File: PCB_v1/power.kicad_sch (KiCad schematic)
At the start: 23 parts, among them J2 S2B-PH-K-SLFSN, J3 Conn_01x05_Pin, J4 Conn_01x05_Pin, U1 BQ25185DLHR, U2 BQ27441-G1

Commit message: PCB changes before changing Seth's clock
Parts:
- U2: footprint Texas_S-PDSO-N12 -> Package_SON:Texas_S-PDSO-N12
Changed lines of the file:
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@@
 			)
 		)
-		(property "Description" "WSL0805R0100FEA1"
+		(property "Description" "Resistor"
 			(at 69.85 118.11 0)
 			(effects
@@
 			)
 		)
-		(property "Footprint" "Texas_S-PDSO-N12"
+		(property "Footprint" "Package_SON:Texas_S-PDSO-N12"
 			(at 101.6 129.54 0)
 			(effects

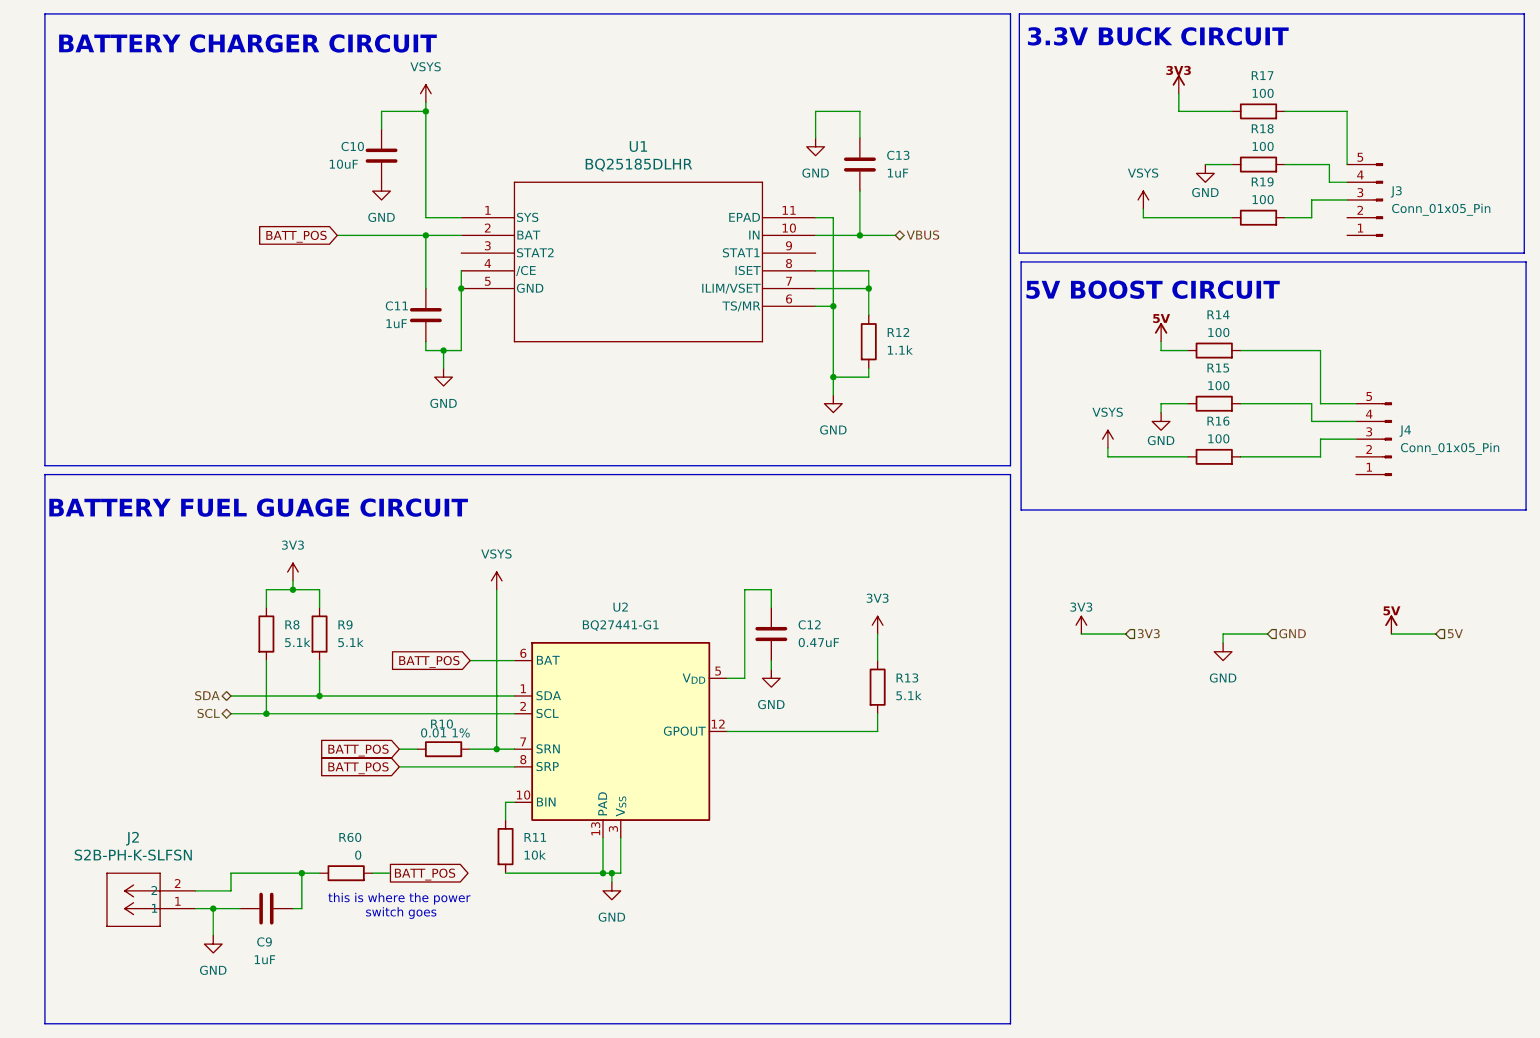
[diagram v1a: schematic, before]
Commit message: Update before adding AGND for the power delivery
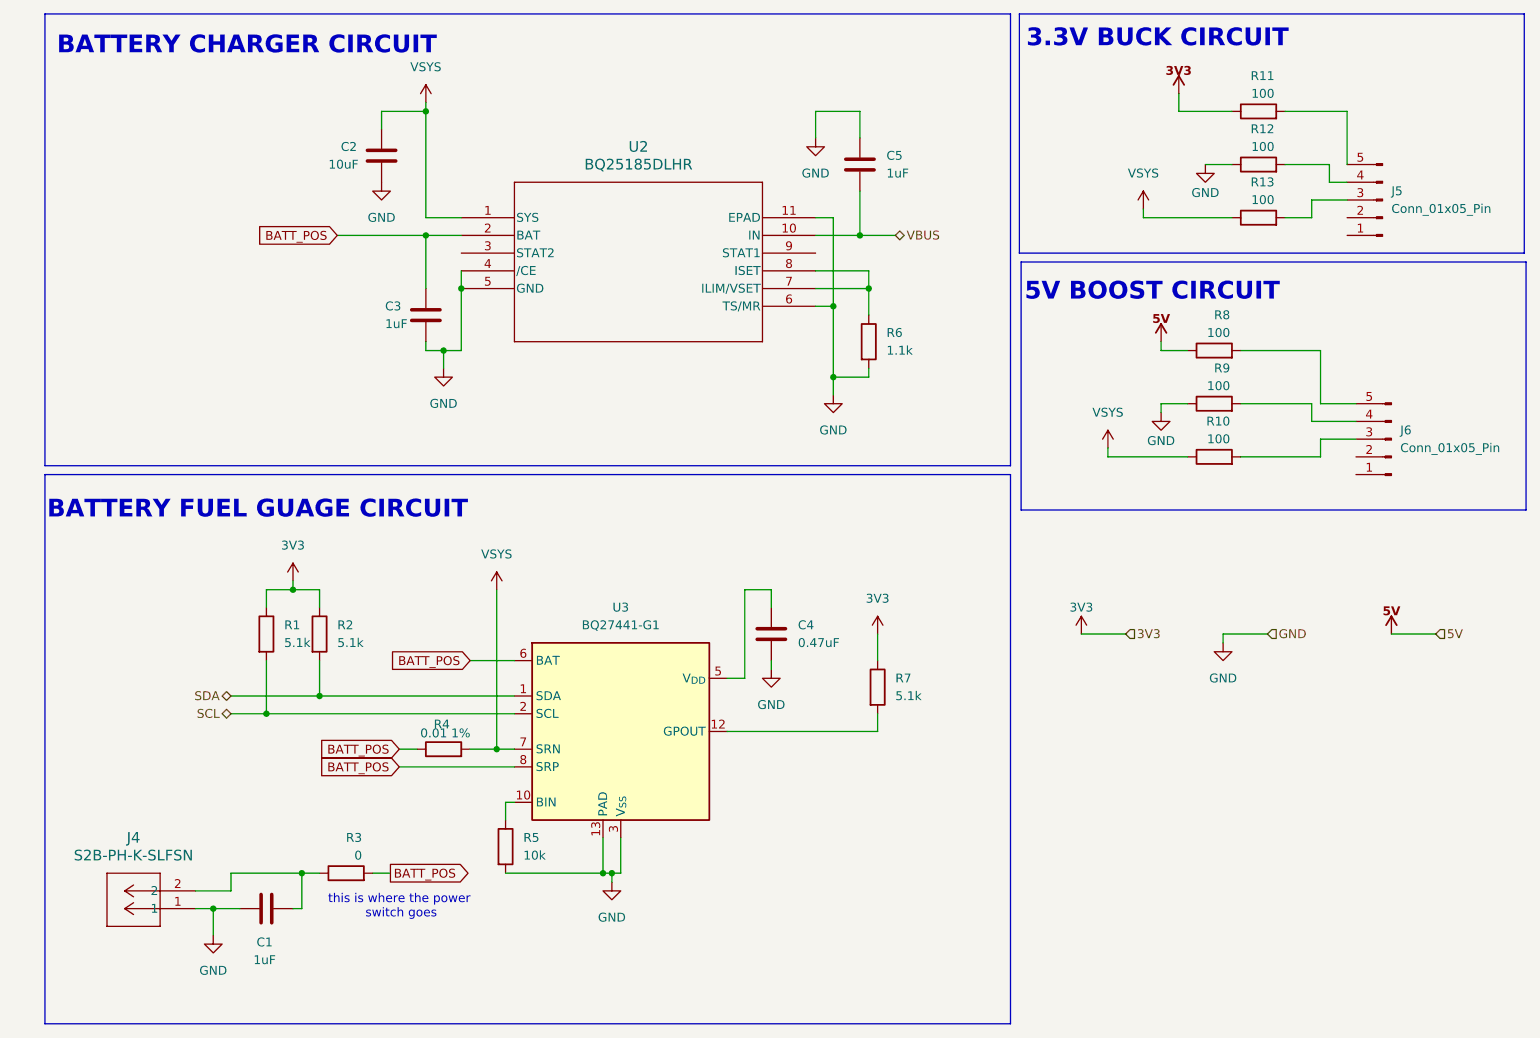
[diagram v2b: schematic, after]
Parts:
- J6: renamed from J4; footprint Connector_PinHeader_1.00mm:PinHeader_1x05_P1.00mm_Vertical -> Connector_PinHeader_2.54mm:PinHeader_1x05_P2.54mm_Vertical
- renumbered C9 to C1, C10 to C2, C11 to C3, C12 to C4, C13 to C5, J2 to J4, J3 to J5, R8 to R1, R16 to R10, R17 to R11, R18 to R12, R19 to R13, R9 to R2, R60 to R3, R10 to R4, R11 to R5, R12 to R6, R13 to R7, R14 to R8, R15 to R9, U1 to U2, U2 to U3

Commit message: Initial placement draft
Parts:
- removed R3: 0, Resistor_SMD:R_0805_2012Metric, symbol Device:R
- added SW1: SW_SPST, Parts_Library:JST_B2B-XH-A, symbol Switch:SW_SPST
- R4: MFP (none) -> WSL0805R0100FEA1
- renumbered R1 to R2, R2 to R3
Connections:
- net BATT_POS: now also SW1.2 (B)
- net GND: no longer R9.1
- net at C1.2, J4.2: now also SW1.1 (A)
- new net AGND: R9.1
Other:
- note added: "The Footprint for the power switch is a 2 pin- 2.54 mm jst connector"
- note removed: "this is where the power switch goes"
